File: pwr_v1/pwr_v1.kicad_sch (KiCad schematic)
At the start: 3 parts

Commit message: Schematic updated
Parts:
- removed J_IR1, J_RF1: Conn_02x04_Counter_Clockwise, symbol Connector_Generic:Conn_02x04_Counter_Clockwise
- renumbered KB to KB1
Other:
- added sheet IR (ir.kicad_sch)
- added sheet RF (rf.kicad_sch)
- sheet Battery Supervisor ports: added B1, B2, B3, B4, B5, B6, G, O1, O2, O3, O4, O5, O6; removed none
- sheet STM32 ports: added BTN_USER, KICKER_DISCHARGE, LED_GREEN, LED_RED, LED_YELLOW, MOTOR1_BREAK, MOTOR1_ENCODER, MOTOR1_PWM, MOTOR1_REVERSE, MOTOR2_BREAK, MOTOR2_ENCODER, MOTOR2_PWM, MOTOR2_REVERSE, MOTOR3_BREAK, MOTOR3_ENCODER, MOTOR3_PWM, MOTOR3_REVERSE, MOTOR4_BREAK, MOTOR4_ENCODER, MOTOR4_PWM, MOTOR4_REVERSE, NRF_CE, NRF_CSN, NRF_IRQ, NRF_MISO, NRF_SCK; removed none
- moved on the sheet: KB1

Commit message: Schematic and layout updated
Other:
- moved on the sheet: KB1

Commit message: Schematic updated
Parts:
- added BAT1: Conn_01x02, TerminalBlock_4Ucon:TerminalBlock_4Ucon_1x02_P3.50mm_Horizontal, symbol Connector_Generic:Conn_01x02
- KB1: value Conn_01x02 -> Conn_01x05; symbol Connector_Generic:Conn_01x02 -> Connector_Generic:Conn_01x05
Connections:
- net STM32/KICKER_DISCHARGE: now also KB1.2 (Pin_2)
- net VBAT: now reaches KB1.1 (Pin_1)
- net VBAT: now also BAT1.2 (Pin_2)
- new net GND: BAT1.1 (Pin_1)
- new net MISO: KB1.3 (Pin_3)
- new net MOSI: KB1.5 (Pin_5)
- new net SCK: KB1.4 (Pin_4)
- no-connect marks 0 -> 27
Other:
- sheet PowerManagement ports: added GND, VBAT; removed none
- sheet RF ports: added 3V3; removed VCC
- sheet STM32 ports: added 5V, CS_NRF, GND, MISO, MOSI, SCK; removed NRF_CSN, NRF_MISO, NRF_SCK

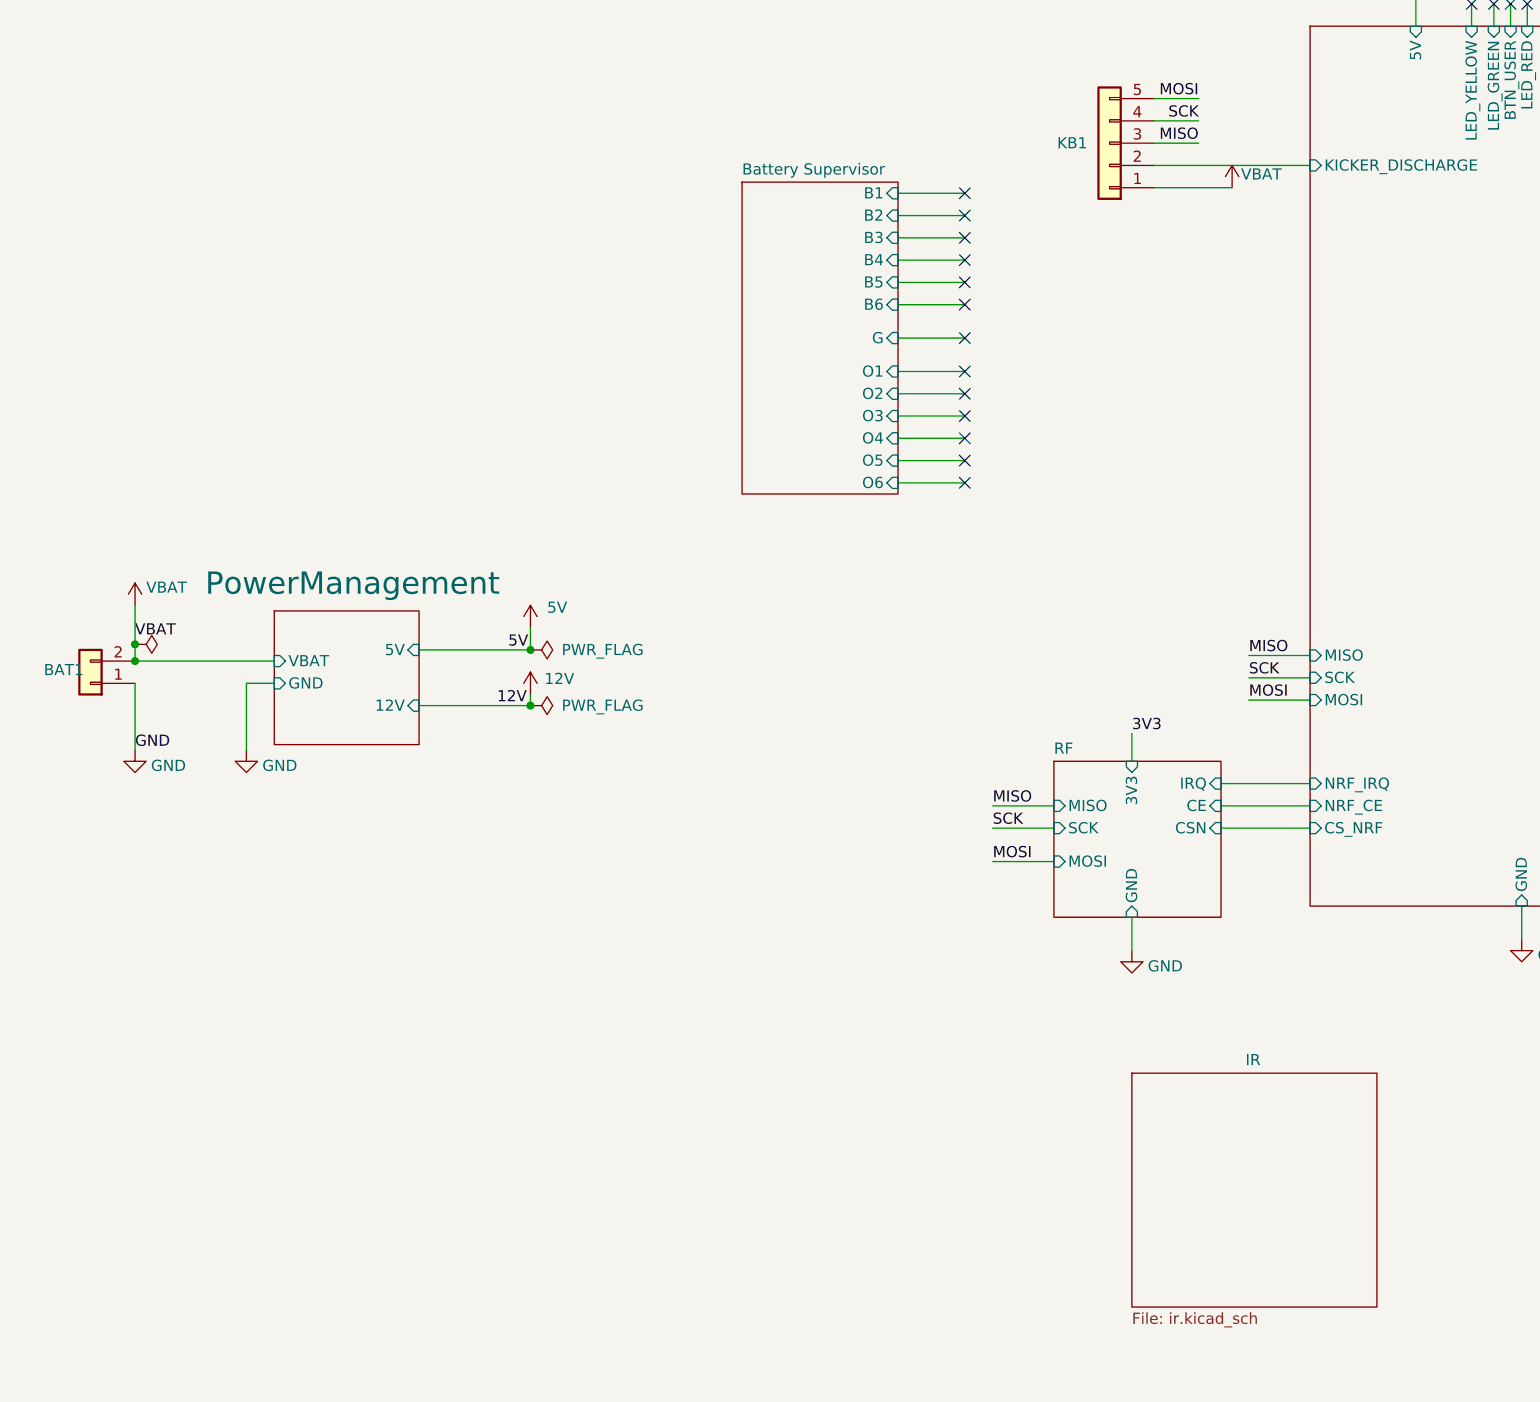
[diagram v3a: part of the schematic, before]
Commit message: Sch and Layout updated; Added batt sup ckt, placed and routed all motor drivers.
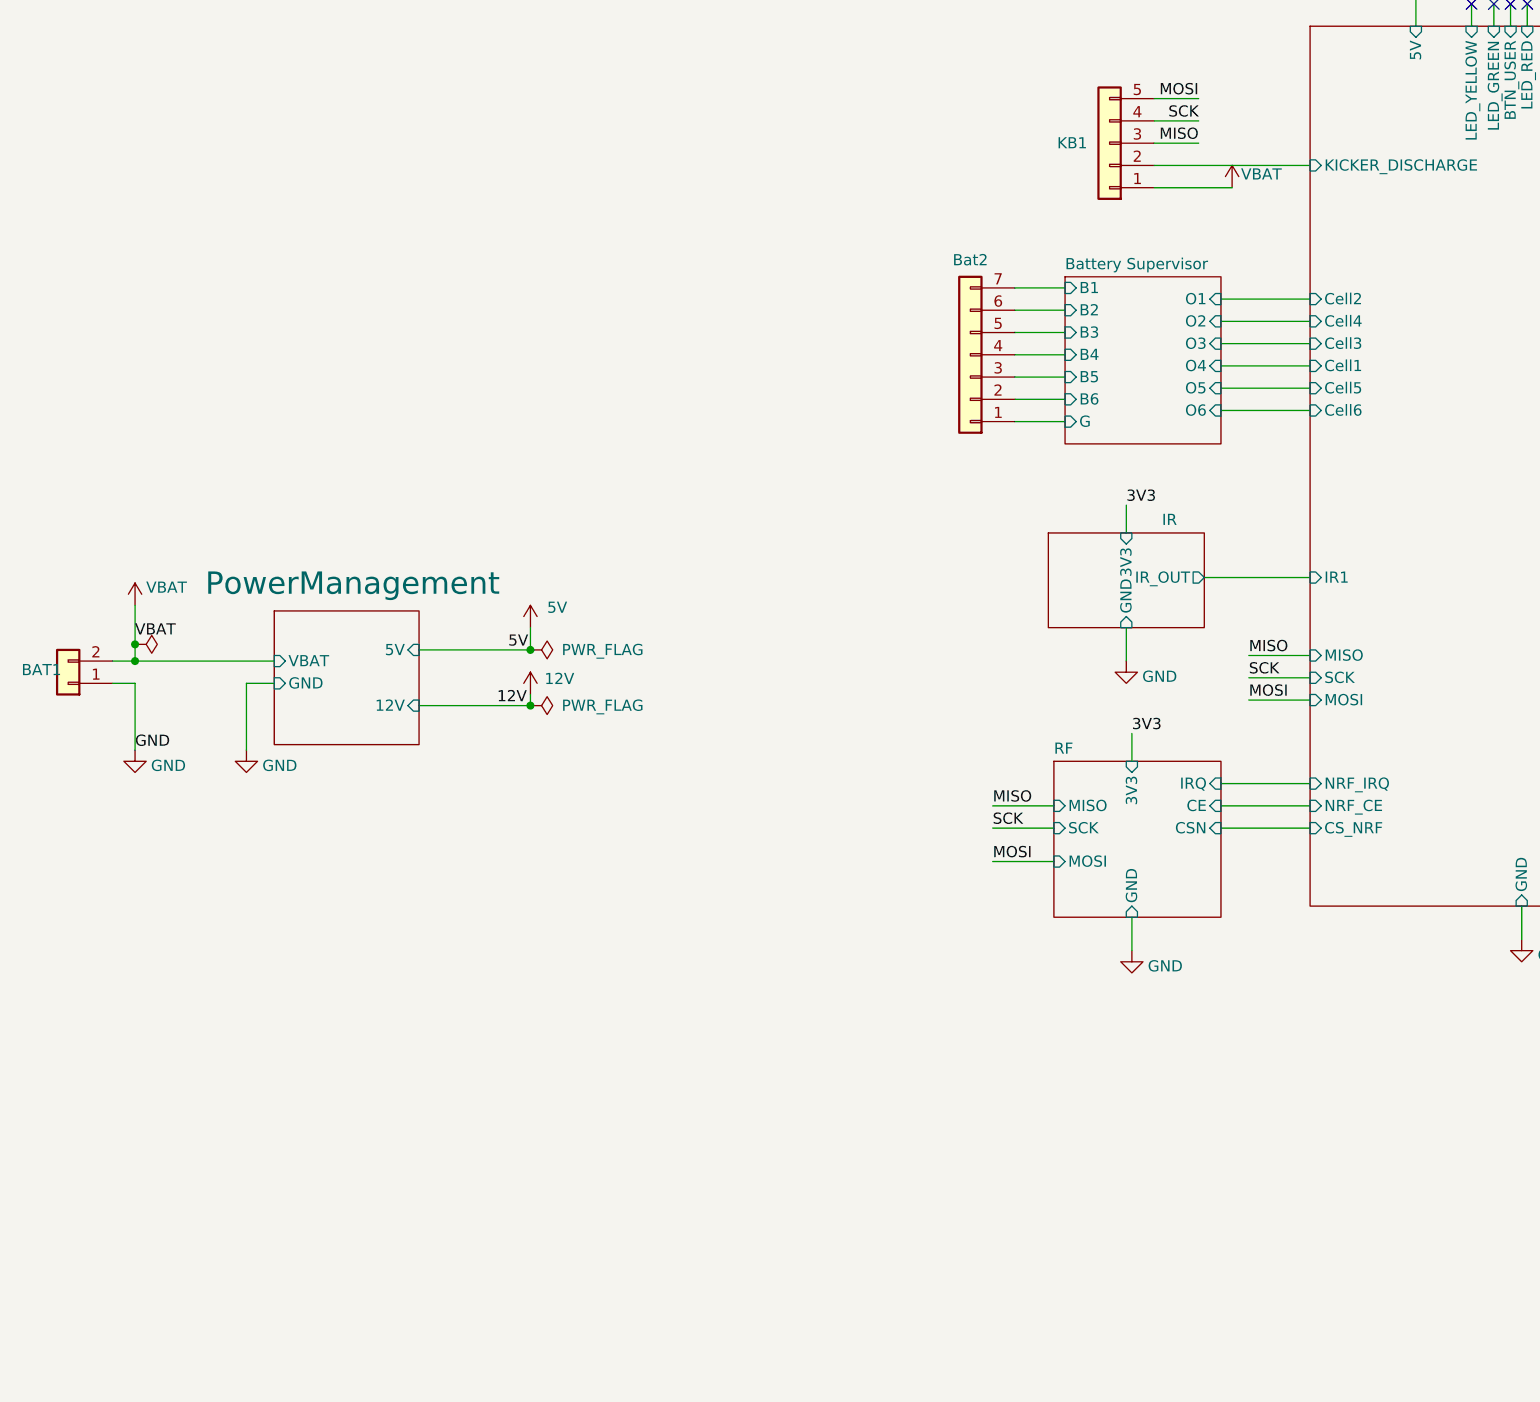
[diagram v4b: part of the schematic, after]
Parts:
- added Bat2: Conn_01x07, symbol Connector_Generic:Conn_01x07
- BAT1: value Conn_01x02 -> XT60; footprint TerminalBlock_4Ucon:TerminalBlock_4Ucon_1x02_P3.50mm_Horizontal -> Connector_AMASS:AMASS_XT60-M_1x02_P7.20mm_Vertical
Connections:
- net Battery Supervisor/B1: now also Bat2.7 (Pin_7)
- net Battery Supervisor/B2: now also Bat2.6 (Pin_6)
- net Battery Supervisor/B3: now also Bat2.5 (Pin_5)
- net Battery Supervisor/B4: now also Bat2.4 (Pin_4)
- net Battery Supervisor/B5: now also Bat2.3 (Pin_3)
- net Battery Supervisor/B6: now also Bat2.2 (Pin_2)
- net Battery Supervisor/G: now also Bat2.1 (Pin_1)
- no-connect marks 27 -> 14
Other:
- sheet IR ports: added 3V3, GND, IR_OUT; removed none
- sheet STM32 ports: added Cell1, Cell2, Cell3, Cell4, Cell5, Cell6, IR1; removed none
- moved on the sheet: BAT1

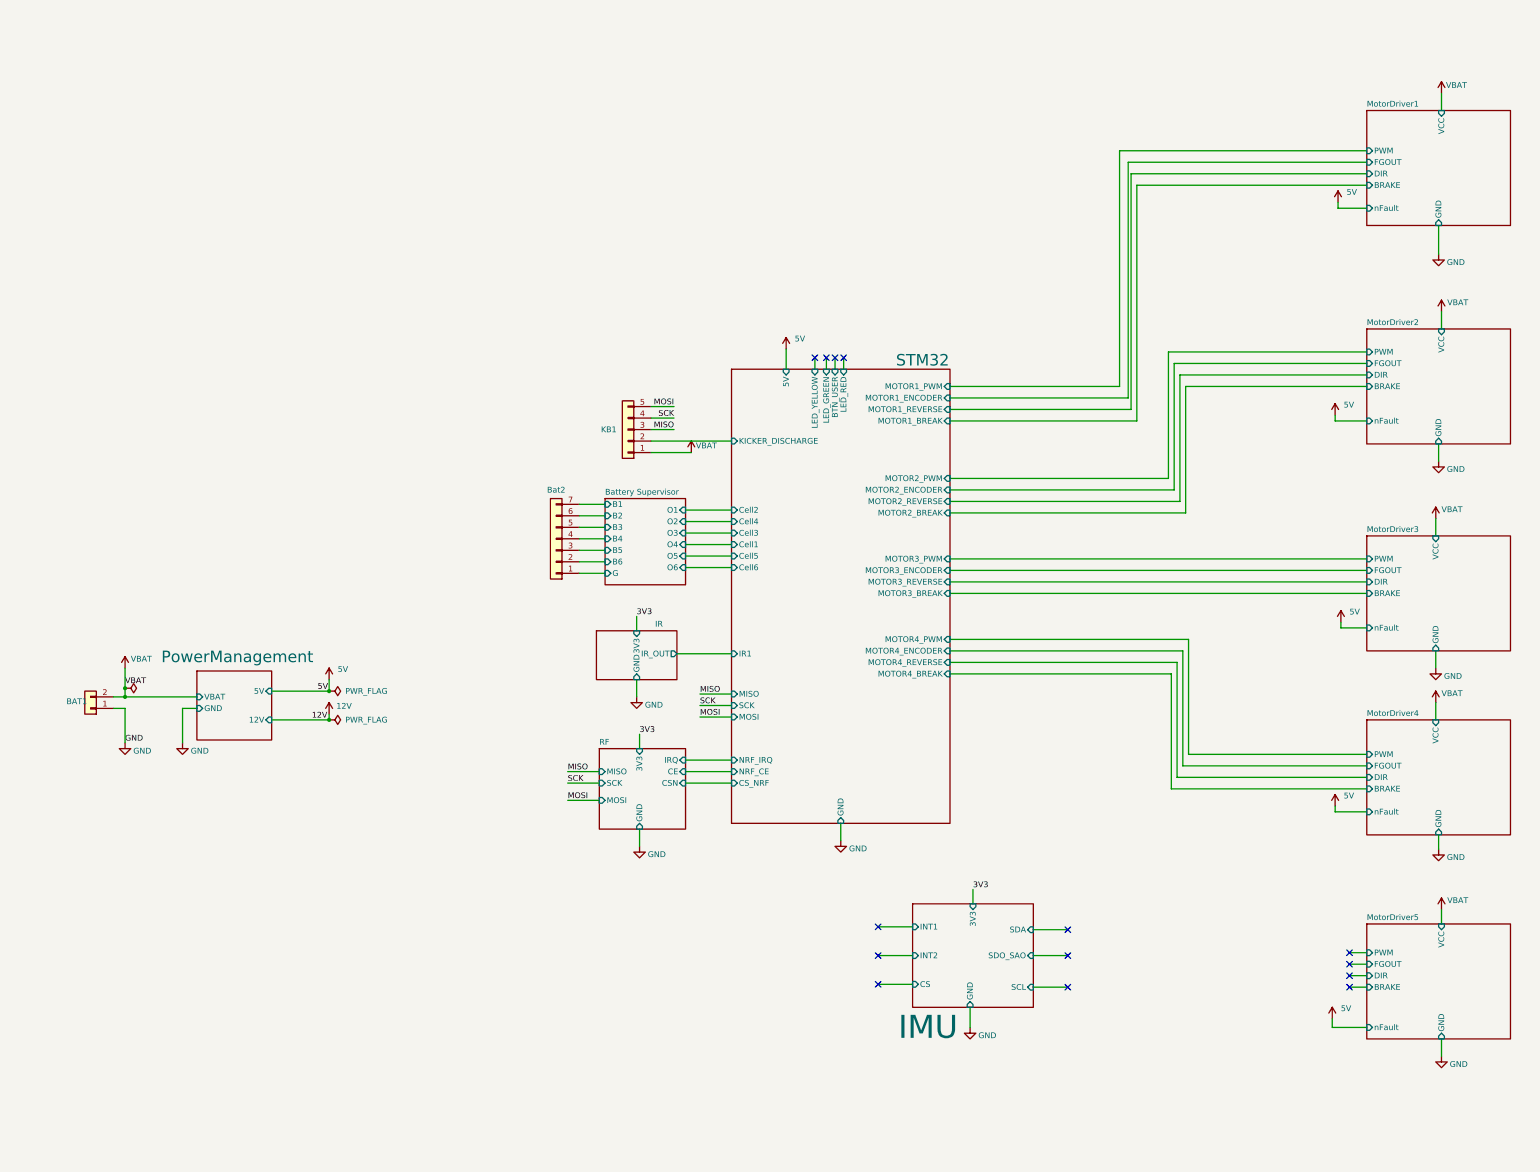
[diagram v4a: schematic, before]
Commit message: Schematic updated; Layout updated; STM PinMappings file added
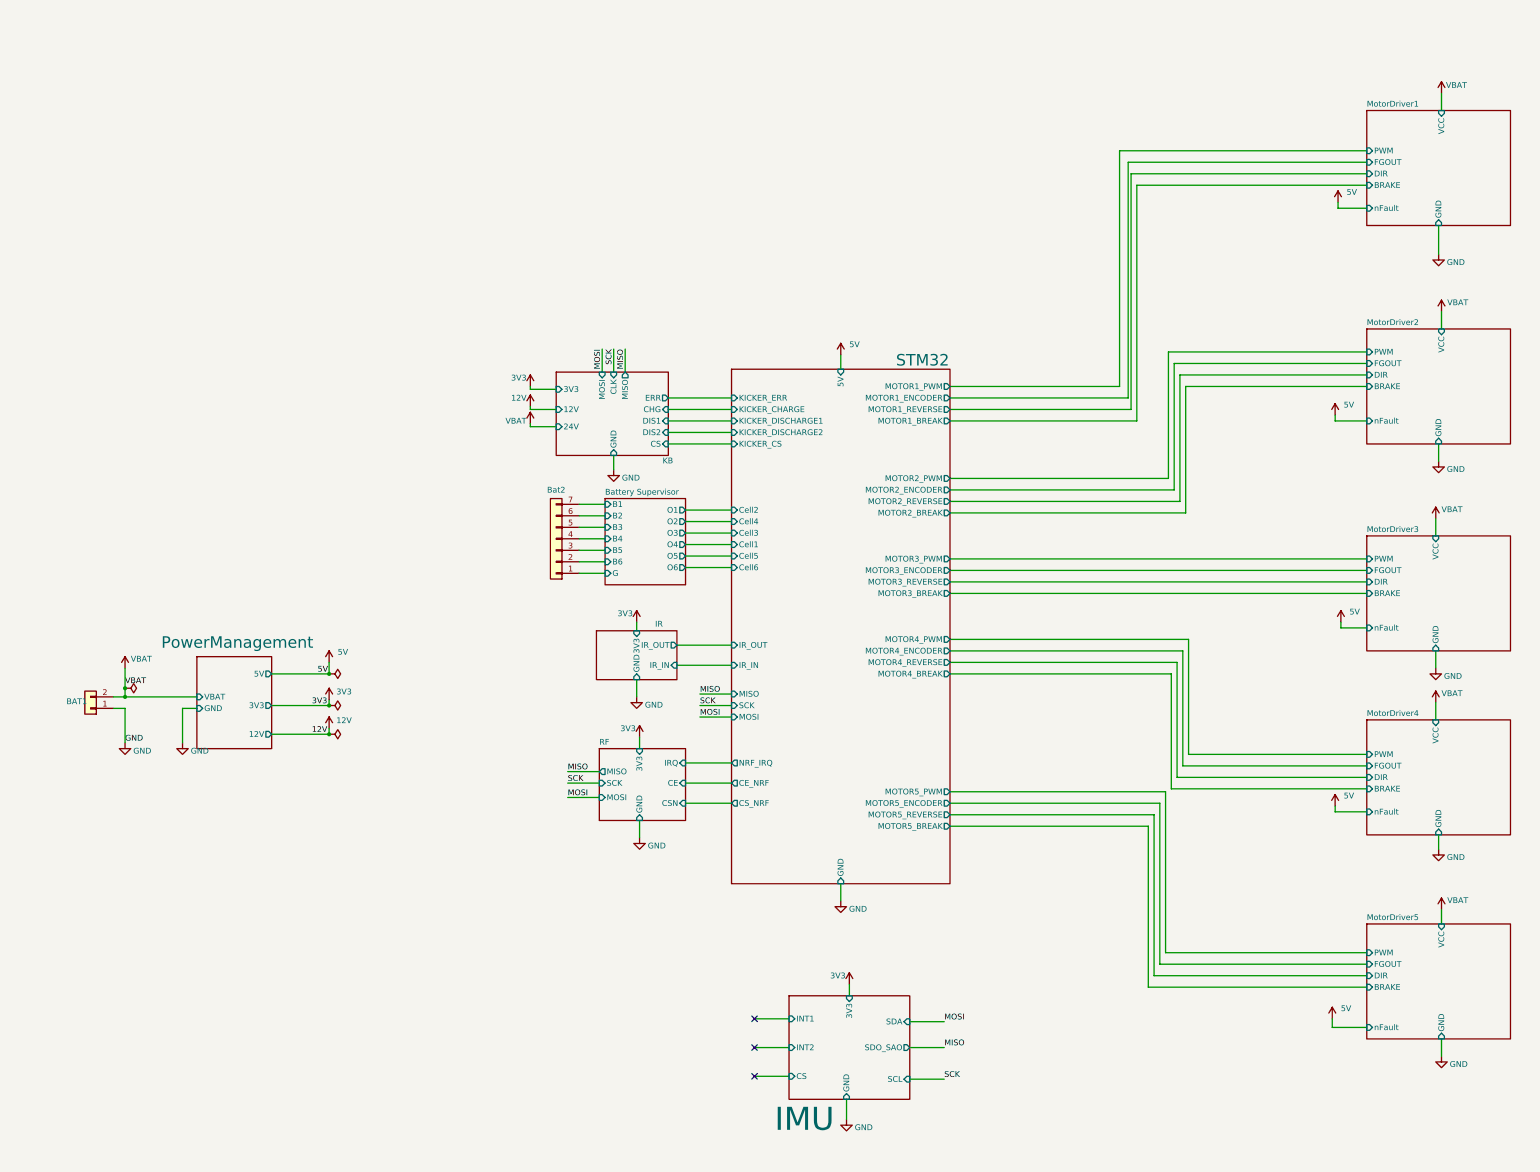
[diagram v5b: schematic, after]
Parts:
- removed KB1: Conn_01x05, symbol Connector_Generic:Conn_01x05
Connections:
- no-connect marks 14 -> 3
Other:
- added sheet KB (kb.kicad_sch)
- sheet IR ports: added IR_IN; removed none
- sheet PowerManagement ports: added 3V3; removed none
- sheet STM32 ports: added CE_NRF, IR_IN, IR_OUT, KICKER_CHARGE, KICKER_CS, KICKER_DISCHARGE1, KICKER_DISCHARGE2, KICKER_ERR, MOTOR5_BREAK, MOTOR5_ENCODER, MOTOR5_PWM, MOTOR5_REVERSE; removed BTN_USER, IR1, KICKER_DISCHARGE, LED_GREEN, LED_RED, LED_YELLOW, NRF_CE
